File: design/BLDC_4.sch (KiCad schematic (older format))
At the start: 26 parts, among them K1 SERVO, P1 HALL/Encoder, P101 CANBUS, P3 PWR_COMM, P4 IN+, P5 IN-, P6 MOTOR1, P7 MOTOR2, P9 MOTOR3, X1 MINI-USB-SHIELD-32005-201

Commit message: Version 0.1 :godmode:
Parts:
- removed C3: 100n, CRF1:SMD-0603_c, symbol C-RESCUE-BLDC_4
- removed K1: SERVO, CRF1:pinhead-1X03, symbol CONN_3
- removed P1: HALL/Encoder, CRF1:MICRO_JST_6, symbol CONN_6
- removed P101: CANBUS, JST conn:b4b-ph-kl, symbol CONN_4
- removed R5: 2k2, CRF1:SMD-0603_r, symbol R-RESCUE-BLDC_4
- removed R53, R54: SHUNT, CRF1:WSLP2726, symbol SHUNT
- removed X1: MINI-USB-SHIELD-32005-201, CRF1:USB-UX60R-MB-5ST, symbol MINI-USB-SCHIELD-32005-201
- added J1: Conn_01x04, Connector_PinHeader_2.54mm:PinHeader_1x04_P2.54mm_Vertical, symbol Connector_Generic:Conn_01x04
- added R10, R9: 1mOhm, Resistor_SMD:R_0612_1632Metric, symbol Device:R
- C1: renamed from C2; footprint CRF1:SMD-0603_c -> Capacitor_SMD:C_0603_1608Metric_Pad1.05x0.95mm_HandSolder; symbol C-RESCUE-BLDC_4 -> BLDC_4-rescue:C-RESCUE-BLDC_4
- D1: renamed from D2; footprint LEDs:LED-0603 -> LED_SMD:LED_0603_1608Metric; symbol LED-RESCUE-BLDC_4 -> BLDC_4-rescue:LED-RESCUE-BLDC_4
- D2: renamed from D1; footprint LEDs:LED-0603 -> LED_SMD:LED_0603_1608Metric; symbol LED-RESCUE-BLDC_4 -> BLDC_4-rescue:LED-RESCUE-BLDC_4
- D3: footprint LEDs:LED-0603 -> LED_SMD:LED_0603_1608Metric; symbol LED-RESCUE-BLDC_4 -> BLDC_4-rescue:LED-RESCUE-BLDC_4
- P1: renamed from P3; footprint CRF1:b7b-ph-kl -> Connector_JST:JST_PH_B7B-PH-K_1x07_P2.00mm_Vertical; symbol CONN_01X07 -> BLDC_4-rescue:CONN_01X07
- P2: renamed from P4; symbol CONN_1 -> BLDC_4-rescue:CONN_1
- P3: renamed from P5; symbol CONN_1 -> BLDC_4-rescue:CONN_1
- P4: renamed from P9; symbol CONN_1 -> BLDC_4-rescue:CONN_1
- P5: renamed from P7; symbol CONN_1 -> BLDC_4-rescue:CONN_1
- P6: symbol CONN_1 -> BLDC_4-rescue:CONN_1
- R1: renamed from R3; footprint CRF1:SMD-0603_r -> Resistor_SMD:R_0603_1608Metric; symbol R-RESCUE-BLDC_4 -> BLDC_4-rescue:R-RESCUE-BLDC_4
- R2: renamed from R4; footprint CRF1:SMD-0603_r -> Resistor_SMD:R_0603_1608Metric; symbol R-RESCUE-BLDC_4 -> BLDC_4-rescue:R-RESCUE-BLDC_4
- R3: renamed from R6; footprint CRF1:SMD-0603_r -> Resistor_SMD:R_0603_1608Metric; symbol R-RESCUE-BLDC_4 -> BLDC_4-rescue:R-RESCUE-BLDC_4
- R4: renamed from R103; footprint CRF1:SMD-0603_r -> Resistor_SMD:R_0603_1608Metric; symbol R-RESCUE-BLDC_4 -> BLDC_4-rescue:R-RESCUE-BLDC_4
- R5: renamed from R104; footprint CRF1:SMD-0603_r -> Resistor_SMD:R_0603_1608Metric; symbol R-RESCUE-BLDC_4 -> BLDC_4-rescue:R-RESCUE-BLDC_4
- R6: renamed from R38; footprint CRF1:SMD-0603_r -> Resistor_SMD:R_0603_1608Metric; symbol R-RESCUE-BLDC_4 -> BLDC_4-rescue:R-RESCUE-BLDC_4
- R7: renamed from R37; footprint CRF1:SMD-0603_r -> Resistor_SMD:R_0603_1608Metric; symbol R-RESCUE-BLDC_4 -> BLDC_4-rescue:R-RESCUE-BLDC_4
- R8: renamed from R22; footprint CRF1:SMD-0603_r -> Resistor_SMD:R_0603_1608Metric; symbol R-RESCUE-BLDC_4 -> BLDC_4-rescue:R-RESCUE-BLDC_4
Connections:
- wire segments 91 -> 84
- no-connect marks 1 -> 0
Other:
- note removed: "100R if used as\nservo output"

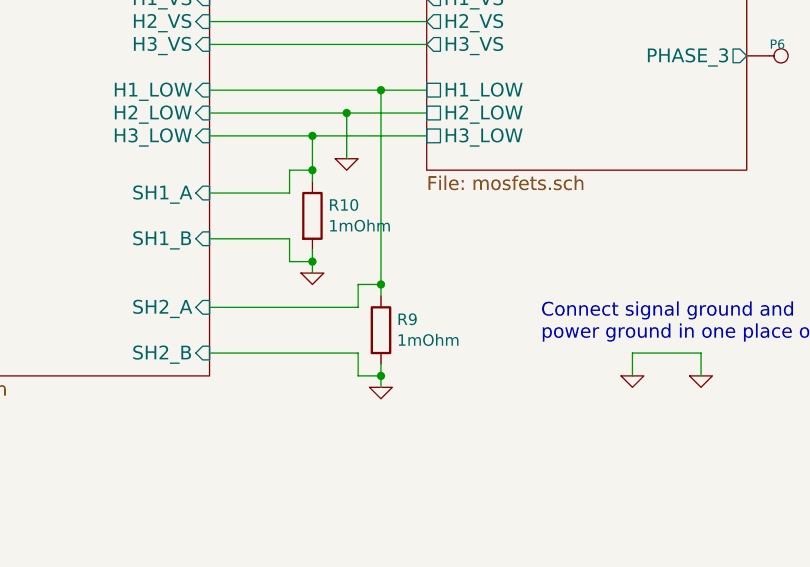
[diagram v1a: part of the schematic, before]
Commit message: Strengthening fills for output stage. Adding GND Fill
More to come :godmode:
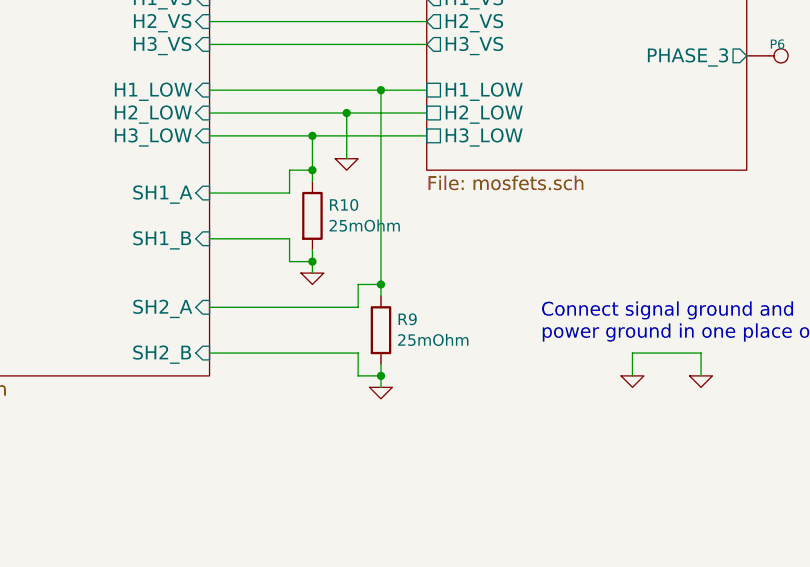
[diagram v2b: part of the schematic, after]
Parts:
- R10, R9: value 1mOhm -> 25mOhm
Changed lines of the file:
@@
 P 8150 4350
 F 0 "R10" H 8220 4396 50  0000 L CNN
-F 1 "1mOhm" H 8220 4305 50  0000 L CNN
+F 1 "25mOhm" H 8220 4305 50  0000 L CNN
 F 2 "Resistor_SMD:R_0612_1632Metric" V 8080 4350 50  0001 C CNN
 F 3 "~" H 8150 4350 50  0001 C CNN
@@
 P 8450 4850
 F 0 "R9" H 8520 4896 50  0000 L CNN
-F 1 "1mOhm" H 8520 4805 50  0000 L CNN
+F 1 "25mOhm" H 8520 4805 50  0000 L CNN
 F 2 "Resistor_SMD:R_0612_1632Metric" V 8380 4850 50  0001 C CNN
 F 3 "~" H 8450 4850 50  0001 C CNN

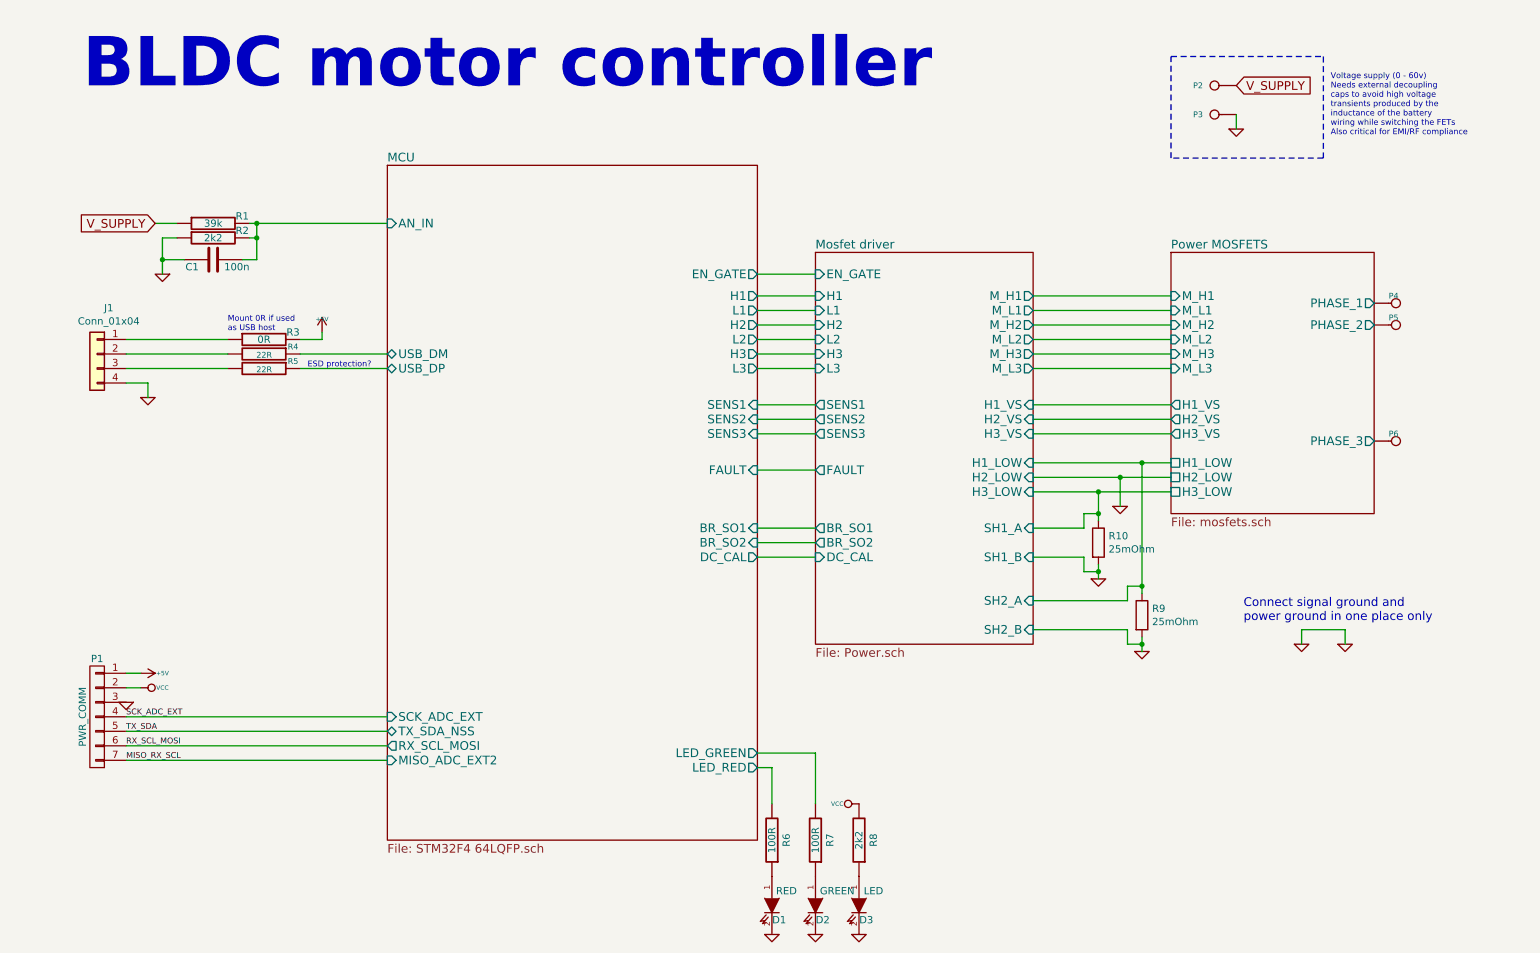
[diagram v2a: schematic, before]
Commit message: Added BOM and reworked component naming to be inline with old VESC names
:^)
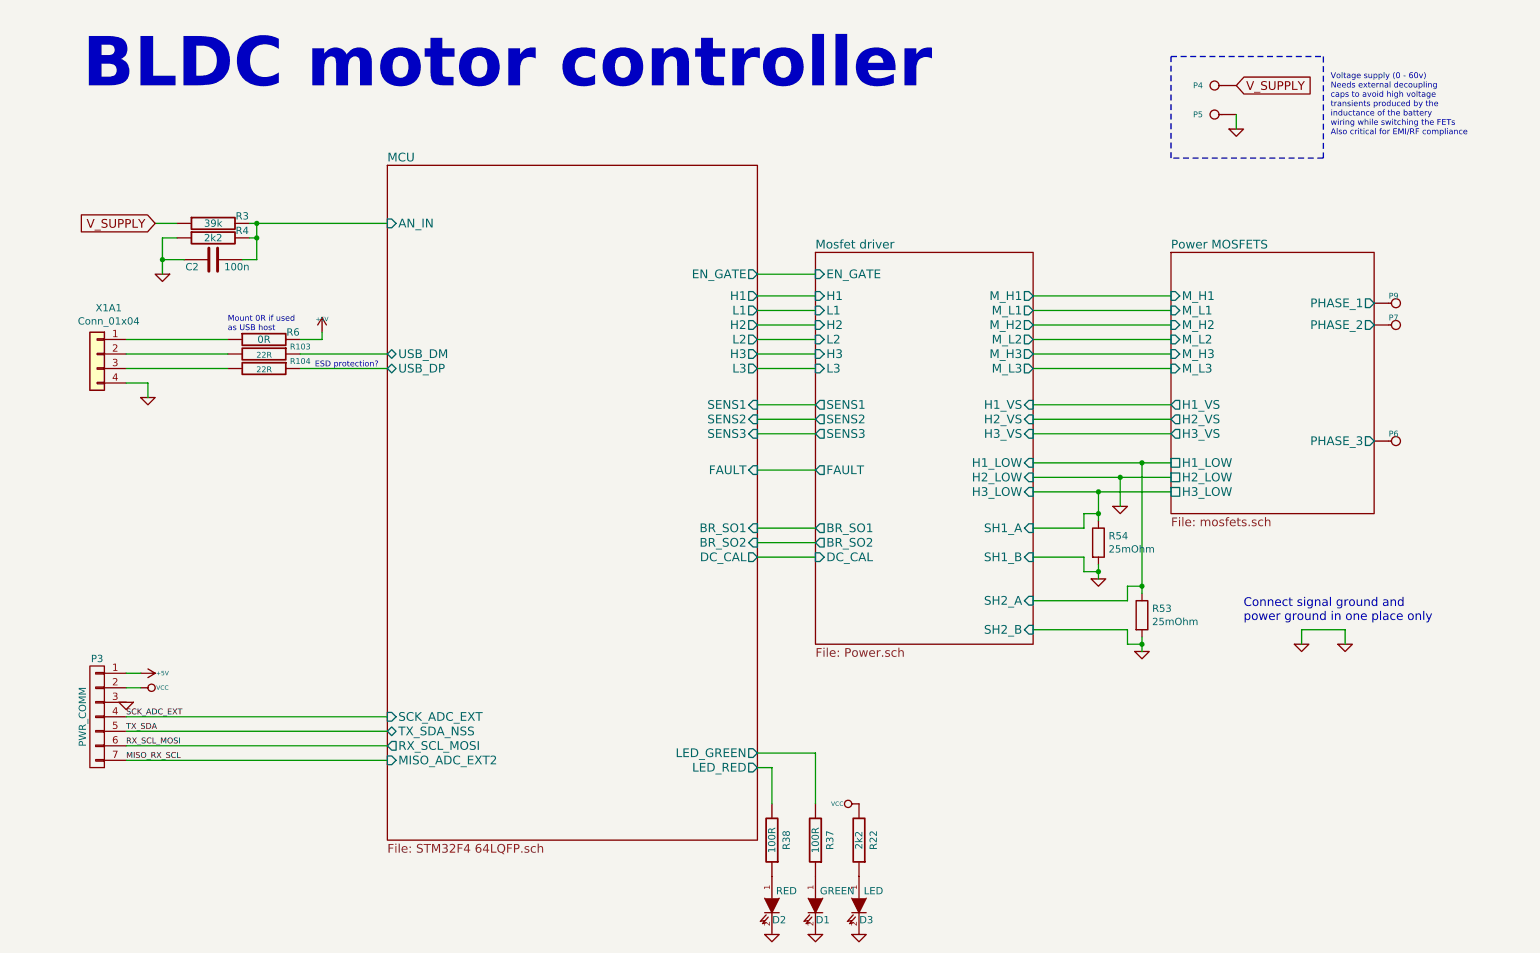
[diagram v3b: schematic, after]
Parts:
- renumbered C1 to C2, D2 to D1, D1 to D2, P1 to P3, P2 to P4, P3 to P5, P5 to P7, P4 to P9, R4 to R103, R5 to R104, R8 to R22, R1 to R3, R7 to R37, R6 to R38, R2 to R4, R9 to R53, R10 to R54, R3 to R6, J1 to X1A1
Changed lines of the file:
@@
 $EndDescr
 $Comp
-L BLDC_4-rescue:C-RESCUE-BLDC_4 C1
+L BLDC_4-rescue:C-RESCUE-BLDC_4 C2
 U 1 1 522DA0B3
 P 2050 2400
-F 0 "C1" V 2100 2500 50  0000 L CNN
+F 0 "C2" V 2100 2500 50  0000 L CNN
 F 1 "100n" V 2100 2150 50  0000 L CNN
 F 2 "Capacitor_SMD:C_0603_1608Metric_Pad1.05x0.95mm_HandSolder" H 2050 2400 60  0001 C CNN
@@
 $EndComp
 $Comp
-L BLDC_4-rescue:R-RESCUE-BLDC_4 R2
+L BLDC_4-rescue:R-RESCUE-BLDC_4 R4
 U 1 1 522DA0D4
 P 2050 2250
-F 0 "R2" V 2000 2050 50  0000 C CNN
+F 0 "R4" V 2000 2050 50  0000 C CNN
 F 1 "2k2" V 2050 2250 50  0000 C CNN
 F 2 "Resistor_SMD:R_0603_1608Metric" H 2050 2250 60  0001 C CNN
@@
 $EndComp
 $Comp
-L BLDC_4-rescue:R-RESCUE-BLDC_4 R1
+L BLDC_4-rescue:R-RESCUE-BLDC_4 R3
 U 1 1 522DA0DA
 P 2050 2150
-F 0 "R1" V 2000 1950 50  0000 C CNN
+F 0 "R3" V 2000 1950 50  0000 C CNN
 F 1 "39k" V 2050 2150 50  0000 C CNN
 F 2 "Resistor_SMD:R_0603_1608Metric" H 2050 2150 60  0001 C CNN
@@
 $EndComp
 $Comp
-L BLDC_4-rescue:R-RESCUE-BLDC_4 R3
+L BLDC_4-rescue:R-RESCUE-BLDC_4 R6
 U 1 1 522DA24E
 P 2400 2950
-F 0 "R3" V 2350 2750 50  0000 C CNN
+F 0 "R6" V 2350 2750 50  0000 C CNN
 F 1 "0R" V 2400 2950 50  0000 C CNN
 F 2 "Resistor_SMD:R_0603_1608Metric" H 2400 2950 60  0001 C CNN
@@
 Text Notes 2150 2900 0    40   ~ 0
 Mount 0R if used\nas USB host
-Text Notes 2700 3150 0    40   ~ 0
+Text Notes 2750 3150 0    40   ~ 0
 ESD protection?\n
 $Sheet
@@
 $EndComp
 $Comp
-L BLDC_4-rescue:CONN_1 P3
+L BLDC_4-rescue:CONN_1 P5
 U 1 1 53FA5B63
 P 8950 1400
-F 0 "P3" H 9030 1400 40  0000 L CNN
+F 0 "P5" H 9030 1400 40  0000 L CNN
 F 1 "IN-" H 8950 1455 30  0001 C CNN
 F 2 "CRF1:1PAD_4x5mm" H 8950 1400 60  0001 C CNN
@@
 $EndComp
 $Comp
-L BLDC_4-rescue:CONN_1 P2
+L BLDC_4-rescue:CONN_1 P4
 U 1 1 53FA5B6A
 P 8950 1200
-F 0 "P2" H 9030 1200 40  0000 L CNN
+F 0 "P4" H 9030 1200 40  0000 L CNN
 F 1 "IN+" H 8950 1255 30  0001 C CNN
 F 2 "CRF1:1PAD_4x5mm" H 8950 1200 60  0001 C CNN
@@
 $EndComp
 $Comp
-L BLDC_4-rescue:CONN_1 P4
+L BLDC_4-rescue:CONN_1 P9
 U 1 1 53FA5B71
 P 10200 2700
-F 0 "P4" H 10150 2750 40  0000 L CNN
+F 0 "P9" H 10150 2750 40  0000 L CNN
 F 1 "MOTOR3" H 10200 2755 30  0001 C CNN
 F 2 "CRF1:1PAD_4x5mm" H 10200 2700 60  0001 C CNN
@@
 $EndComp
 $Comp
-L BLDC_4-rescue:CONN_1 P5
+L BLDC_4-rescue:CONN_1 P7
 U 1 1 53FA5B78
 P 10200 2850
-F 0 "P5" H 10150 2900 40  0000 L CNN
+F 0 "P7" H 10150 2900 40  0000 L CNN
 F 1 "MOTOR2" H 10200 2905 30  0001 C CNN
 F 2 "CRF1:1PAD_4x5mm" H 10200 2850 60  0001 C CNN
@@
 $EndBitmap
 $Comp
-L BLDC_4-rescue:R-RESCUE-BLDC_4 R4
+L BLDC_4-rescue:R-RESCUE-BLDC_4 R103
 U 1 1 53FCA251
 P 2400 3050
-F 0 "R4" V 2350 3250 40  0000 C CNN
+F 0 "R103" V 2350 3300 40  0000 C CNN
 F 1 "22R" V 2407 3051 40  0000 C CNN
 F 2 "Resistor_SMD:R_0603_1608Metric" V 2330 3050 30  0001 C CNN
@@
 $EndComp
 $Comp
-L BLDC_4-rescue:R-RESCUE-BLDC_4 R5
+L BLDC_4-rescue:R-RESCUE-BLDC_4 R104
 U 1 1 53FCA272
 P 2400 3150
-F 0 "R5" V 2350 3350 40  0000 C CNN
+F 0 "R104" V 2350 3400 40  0000 C CNN
 F 1 "22R" V 2407 3151 40  0000 C CNN
 F 2 "Resistor_SMD:R_0603_1608Metric" V 2330 3150 30  0001 C CNN
@@
 Voltage supply (0 - 60v)\nNeeds external decoupling\ncaps to avoid high voltage\ntransients produced by the\ninductance of the battery\nwiring while switching the FETs\nAlso critical for EMI/RF compliance
 $Comp
-L BLDC_4-rescue:R-RESCUE-BLDC_4 R6
+L BLDC_4-rescue:R-RESCUE-BLDC_4 R38
 U 1 1 53FC020B
 P 5900 6400
-F 0 "R6" V 5800 6400 50  0000 C CNN
+F 0 "R38" V 5800 6400 50  0000 C CNN
 F 1 "100R" V 5900 6400 50  0000 C CNN
 F 2 "Resistor_SMD:R_0603_1608Metric" H 5900 6400 60  0001 C CNN
@@
 $EndComp
 $Comp
-L BLDC_4-rescue:LED-RESCUE-BLDC_4 D1
+L BLDC_4-rescue:LED-RESCUE-BLDC_4 D2
 U 1 1 53FC0212
 P 5900 6850
-F 0 "D1" V 6000 6900 50  0000 C CNN
+F 0 "D2" V 6000 6900 50  0000 C CNN
 F 1 "RED" V 5800 6950 50  0000 C CNN
 F 2 "LED_SMD:LED_0603_1608Metric" H 5900 6850 60  0001 C CNN
@@
 $EndComp
 $Comp
-L BLDC_4-rescue:R-RESCUE-BLDC_4 R7
+L BLDC_4-rescue:R-RESCUE-BLDC_4 R37
 U 1 1 53FC130C
 P 6200 6400
-F 0 "R7" V 6100 6400 50  0000 C CNN
+F 0 "R37" V 6100 6400 50  0000 C CNN
 F 1 "100R" V 6200 6400 50  0000 C CNN
 F 2 "Resistor_SMD:R_0603_1608Metric" H 6200 6400 60  0001 C CNN
@@
 $EndComp
 $Comp
-L BLDC_4-rescue:LED-RESCUE-BLDC_4 D2
+L BLDC_4-rescue:LED-RESCUE-BLDC_4 D1
 U 1 1 53FC1313
 P 6200 6850
-F 0 "D2" V 6300 6900 50  0000 C CNN
+F 0 "D1" V 6300 6900 50  0000 C CNN
 F 1 "GREEN" V 6100 7000 50  0000 C CNN
 F 2 "LED_SMD:LED_0603_1608Metric" H 6200 6850 60  0001 C CNN
@@
 $EndComp
 $Comp
-L BLDC_4-rescue:R-RESCUE-BLDC_4 R8
+L BLDC_4-rescue:R-RESCUE-BLDC_4 R22
 U 1 1 53FC6A67
 P 6500 6400
-F 0 "R8" V 6400 6400 50  0000 C CNN
+F 0 "R22" V 6400 6400 50  0000 C CNN
 F 1 "2k2" V 6500 6400 50  0000 C CNN
 F 2 "Resistor_SMD:R_0603_1608Metric" H 6500 6400 60  0001 C CNN
@@
 Connect signal ground and\npower ground in one place only
 $Comp
-L BLDC_4-rescue:CONN_01X07 P1
+L BLDC_4-rescue:CONN_01X07 P3
 U 1 1 55D4F5E0
 P 1250 5550
-F 0 "P1" H 1250 5950 50  0000 C CNN
+F 0 "P3" H 1250 5950 50  0000 C CNN
 F 1 "PWR_COMM" V 1350 5550 50  0000 C CNN
 F 2 "Connector_JST:JST_PH_B7B-PH-K_1x07_P2.00mm_Vertical" H 1250 5550 60  0001 C CNN
@@
 	1600 3250 1450 3250
 $Comp
-L Connector_Generic:Conn_01x04 J1
+L Connector_Generic:Conn_01x04 X1A1
 U 1 1 5DA37C90
 P 1250 3050
-F 0 "J1" H 1170 3367 50  0000 C CNN
+F 0 "X1A1" H 1170 3367 50  0000 C CNN
 F 1 "Conn_01x04" H 1170 3276 50  0000 C CNN
 F 2 "Connector_PinHeader_2.54mm:PinHeader_1x04_P2.54mm_Vertical" H 1250 3050 50  0001 C CNN
@@
 $EndComp
 $Comp
-L Device:R R10
+L Device:R R54
 U 1 1 5DAB321E
 P 8150 4350
-F 0 "R10" H 8220 4396 50  0000 L CNN
+F 0 "R54" H 8220 4396 50  0000 L CNN
 F 1 "25mOhm" H 8220 4305 50  0000 L CNN
 F 2 "Resistor_SMD:R_0612_1632Metric" V 8080 4350 50  0001 C CNN
@@
 	8150 4500 8150 4550
 $Comp
-L Device:R R9
+L Device:R R53
 U 1 1 5DAB7459
 P 8450 4850
-F 0 "R9" H 8520 4896 50  0000 L CNN
+F 0 "R53" H 8520 4896 50  0000 L CNN
 F 1 "25mOhm" H 8520 4805 50  0000 L CNN
 F 2 "Resistor_SMD:R_0612_1632Metric" V 8380 4850 50  0001 C CNN
